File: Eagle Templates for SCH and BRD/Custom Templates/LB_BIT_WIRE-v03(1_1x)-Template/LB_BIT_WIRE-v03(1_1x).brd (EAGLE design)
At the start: 21.4 x 9.4 mm, 6 parts

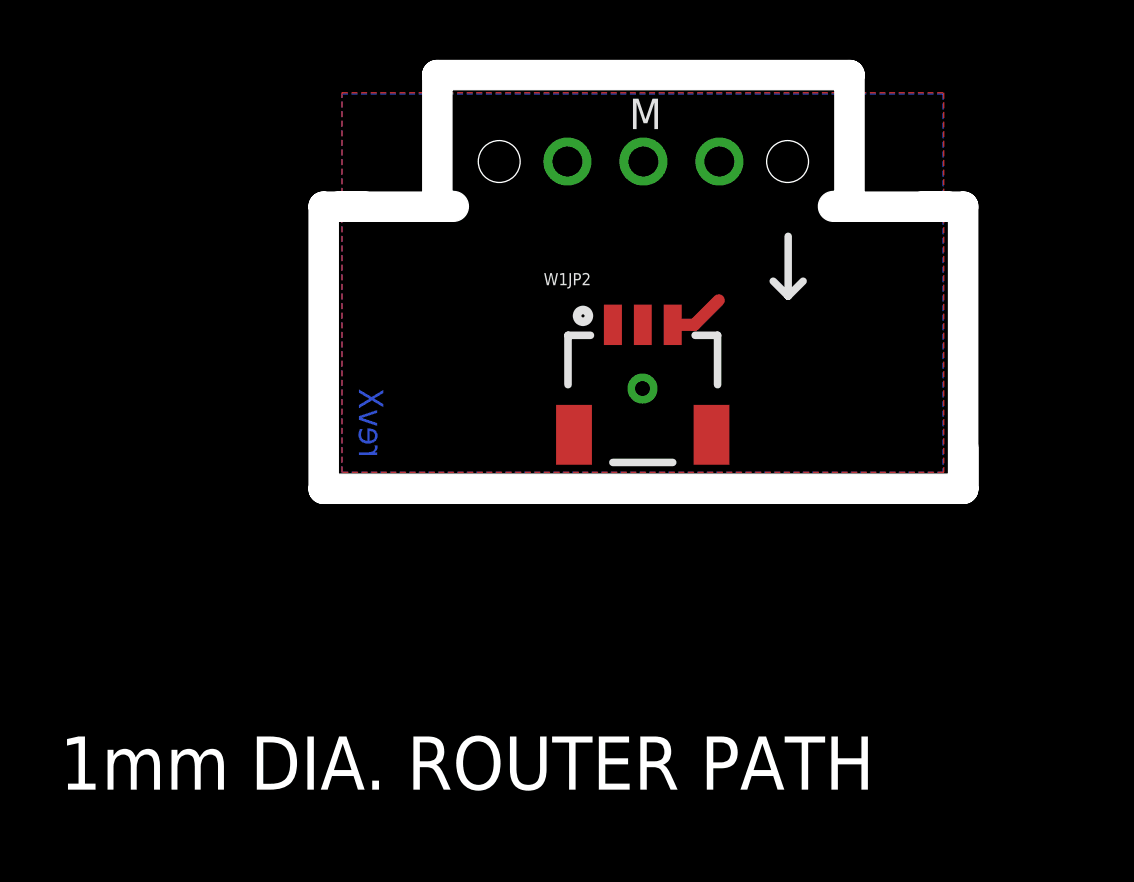
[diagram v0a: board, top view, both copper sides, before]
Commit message: added bitlab logo and made minor changes to board templates. Updated littlebits library.
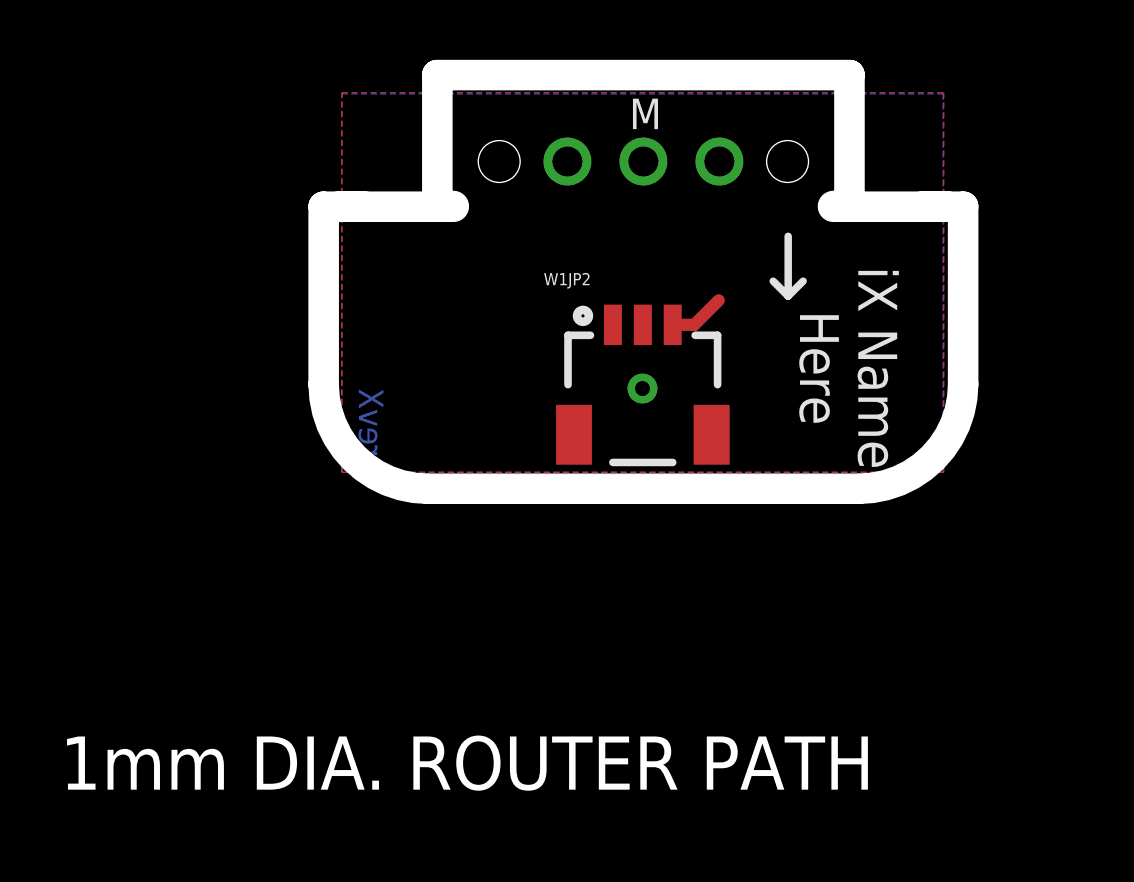
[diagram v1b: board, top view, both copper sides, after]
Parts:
- added U$1: (no value), LITTLEBITS:BITLAB-LOGO
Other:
- outline, holes or cut-outs redrawn
- board text added: "iX Name Here"
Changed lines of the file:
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@@
 <setting verticaltext="up"/>
 </settings>
-<grid distance="0.1" unitdist="mm" unit="mm" style="lines" multiple="1" display="yes" altdistance="0.01" altunitdist="mm" altunit="mm"/>
+<grid distance="0.005" unitdist="mm" unit="mm" style="lines" multiple="1" display="yes" altdistance="0.01" altunitdist="mm" altunit="mm"/>
 <layers>
 <layer number="1" name="Top" color="4" fill="1" visible="yes" active="yes"/>
@@
 <layer number="113" name="extra" color="10" fill="1" visible="yes" active="yes"/>
 <layer number="116" name="Patch_BOT" color="9" fill="4" visible="yes" active="yes"/>
+<layer number="118" name="Rect_Pads" color="7" fill="1" visible="no" active="yes"/>
 <layer number="121" name="_tsilk" color="7" fill="1" visible="yes" active="yes"/>
 <layer number="122" name="_bsilk" color="7" fill="1" visible="yes" active="yes"/>
@@
 <board>
 <plain>
-<wire x1="2.98" y1="0.06" x2="2.98" y2="13.01" width="0" layer="49"/>
+<wire x1="23.38" y1="13.01" x2="23.38" y2="3.06" width="0" layer="49"/>
+<wire x1="23.38" y1="3.06" x2="20.38" y2="0.06" width="0" layer="49" curve="-90"/>
+<wire x1="20.38" y1="0.06" x2="5.98" y2="0.06" width="0" layer="49"/>
+<wire x1="5.98" y1="0.06" x2="2.98" y2="3.06" width="0" layer="49" curve="-90"/>
+<wire x1="2.98" y1="3.06" x2="2.98" y2="13.01" width="0" layer="49"/>
 <wire x1="2.98" y1="13.01" x2="23.38" y2="13.01" width="0" layer="49"/>
-<wire x1="23.38" y1="13.01" x2="23.38" y2="0.06" width="0" layer="49"/>
-<wire x1="23.38" y1="0.06" x2="2.98" y2="0.06" width="0" layer="49"/>
 <dimension x1="6.78" y1="13.51" x2="19.58" y2="13.51" x3="13.18" y3="24.65" textsize="3.5" layer="47" dtype="horizontal"/>
 <dimension x1="23.38" y1="9.01" x2="2.98" y2="9.01" x3="13.18" y3="32.1" textsize="3.5" layer="47" dtype="horizontal"/>
@@
 <wire x1="17.492" y1="11.018" x2="18" y2="11.018" width="0.1016" layer="146"/>
 <text x="-6.3" y="-10.4" size="1.778" layer="46">1mm DIA. ROUTER PATH</text>
-<wire x1="3.01" y1="8.6" x2="3.01" y2="0.15" width="0" layer="20"/>
-<wire x1="23.41" y1="0.15" x2="23.41" y2="8.6" width="0" layer="20"/>
-<wire x1="3.01" y1="0.15" x2="23.41" y2="0.15" width="0" layer="20"/>
-<wire x1="23.91" y1="9.1" x2="23.91" y2="-0.335" width="1" layer="46"/>
+<wire x1="3.01" y1="8.6" x2="3.01" y2="3.15" width="0" layer="20"/>
+<wire x1="3.01" y1="3.15" x2="6.01" y2="0.15" width="0" layer="20" curve="90"/>
+<wire x1="6.01" y1="0.15" x2="20.41" y2="0.15" width="0" layer="20"/>
+<wire x1="20.41" y1="0.15" x2="23.41" y2="3.15" width="0" layer="20" curve="90"/>
+<wire x1="23.41" y1="3.15" x2="23.41" y2="8.6" width="0" layer="20"/>
+<wire x1="23.91" y1="9.1" x2="23.91" y2="3.15" width="1" layer="46"/>
 <wire x1="23.91" y1="9.1" x2="22.515" y2="9.1" width="1" layer="46"/>
-<wire x1="23.91" y1="-0.35" x2="23.91" y2="1.045" width="1" layer="46"/>
-<wire x1="23.91" y1="-0.35" x2="2.51" y2="-0.35" width="1" layer="46"/>
-<wire x1="2.51" y1="-0.35" x2="2.51" y2="9.1" width="1" layer="46"/>
+<wire x1="20.41" y1="-0.35" x2="6.01" y2="-0.35" width="1" layer="46"/>
+<wire x1="6.01" y1="-0.35" x2="2.51" y2="3.15" width="1" layer="46" curve="-90"/>
+<wire x1="2.51" y1="3.15" x2="2.51" y2="9.1" width="1" layer="46"/>
 <wire x1="2.51" y1="9.1" x2="3.905" y2="9.1" width="1" layer="46"/>
 <text x="3.7" y="0.7" size="0.8128" layer="16" font="vector" ratio="12" rot="MR90">revX</text>
+<text x="20.07" y="3.7" size="1.3" layer="21" font="vector" rot="SR270" align="center">iX Name
+Here</text>
+<wire x1="20.41" y1="-0.35" x2="23.91" y2="3.15" width="1" layer="46" curve="90"/>
 </plain>
 <attributes>
@@
 <element name="U$2" library="LITTLEBITS" package="OSHWCREDIT" value="OSHWCREDIT" x="-93.86" y="-61.24"/>
 <element name="FRAME1" library="LITTLEBITS" package="FABDWG01-OHW" value="FRAME-LETTER" x="0" y="0"/>
+<element name="U$1" library="LITTLEBITS" package="BITLAB-LOGO" value="" x="15.325" y="8.27" rot="R270"/>
 </elements>
 <signals>
